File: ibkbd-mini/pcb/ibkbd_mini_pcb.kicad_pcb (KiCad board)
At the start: 2 copper layers, 226 x 106.3 mm, 75 parts

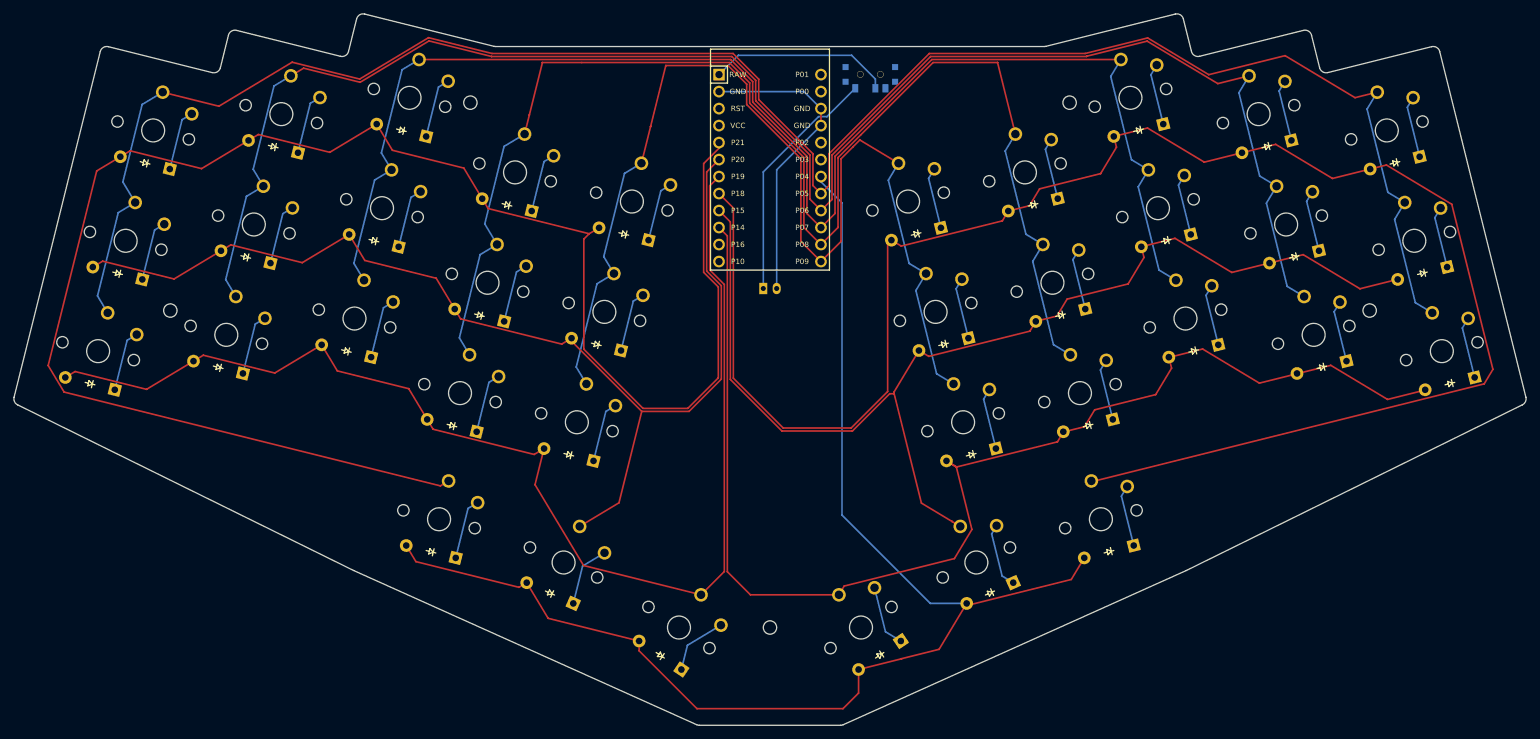
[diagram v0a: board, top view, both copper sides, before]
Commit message: reverse diode direction
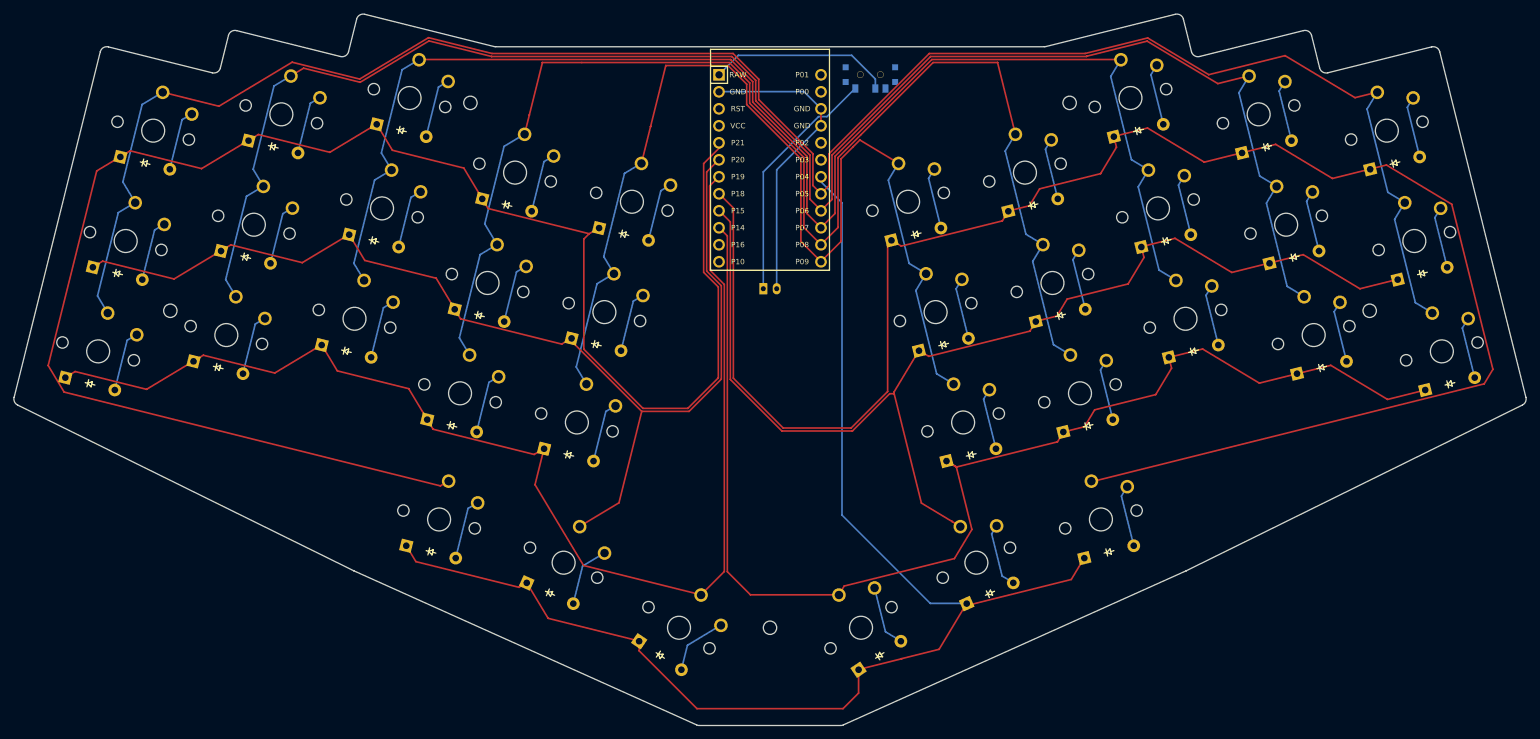
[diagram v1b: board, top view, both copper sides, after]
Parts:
- turned D18 to 14 degrees
- turned D36 to 34 degrees
- turned D33 to -34 degrees
- turned D21 to 14 degrees
- turned D25 to 14 degrees
- turned D11 to -14 degrees
- turned D34 to 14 degrees
- turned D35 to 24 degrees
- turned D15 to -14 degrees
- turned D1 to -14 degrees
- turned D20 to 14 degrees
- turned D19 to 14 degrees
- turned D32 to -24 degrees
- turned D4 to -14 degrees
- turned D24 to 14 degrees
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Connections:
- D1 pad 1: pinky_bottom -> P19
- D1 pad 2: P19 -> pinky_bottom
- D10 pad 1: index_bottom -> P19
- D10 pad 2: P19 -> index_bottom
- D11 pad 1: index_home -> P20
- D11 pad 2: P20 -> index_home
- D12 pad 1: index_top -> P21
- D12 pad 2: P21 -> index_top
- D13 pad 1: inner_bottom -> P19
- D13 pad 2: P19 -> inner_bottom
- D14 pad 1: inner_home -> P20
- D14 pad 2: P20 -> inner_home
- D15 pad 1: inner_top -> P21
- D15 pad 2: P21 -> inner_top
- D16 pad 1: mirror_pinky_bottom -> P14
- D16 pad 2: P14 -> mirror_pinky_bottom
- D17 pad 1: mirror_pinky_home -> P15
- D17 pad 2: P15 -> mirror_pinky_home
- D18 pad 1: mirror_pinky_top -> P18
- D18 pad 2: P18 -> mirror_pinky_top
- D19 pad 1: mirror_ring_bottom -> P14
- D19 pad 2: P14 -> mirror_ring_bottom
- D2 pad 1: pinky_home -> P20
- D2 pad 2: P20 -> pinky_home
- D20 pad 1: mirror_ring_home -> P15
- D20 pad 2: P15 -> mirror_ring_home
- D21 pad 1: mirror_ring_top -> P18
- D21 pad 2: P18 -> mirror_ring_top
- D22 pad 1: mirror_middle_bottom -> P14
- D22 pad 2: P14 -> mirror_middle_bottom
- D23 pad 1: mirror_middle_home -> P15
- D23 pad 2: P15 -> mirror_middle_home
- D24 pad 1: mirror_middle_top -> P18
- D24 pad 2: P18 -> mirror_middle_top
- D25 pad 1: mirror_index_bottom -> P14
- D25 pad 2: P14 -> mirror_index_bottom
- D26 pad 1: mirror_index_home -> P15
- D26 pad 2: P15 -> mirror_index_home
- D27 pad 1: mirror_index_top -> P18
- D27 pad 2: P18 -> mirror_index_top
- D28 pad 1: mirror_inner_bottom -> P14
- D28 pad 2: P14 -> mirror_inner_bottom
- D29 pad 1: mirror_inner_home -> P15
- D29 pad 2: P15 -> mirror_inner_home
- D3 pad 1: pinky_top -> P21
- D3 pad 2: P21 -> pinky_top
- D30 pad 1: mirror_inner_top -> P18
- D30 pad 2: P18 -> mirror_inner_top
- D31 pad 1: inner_key -> P4
- D31 pad 2: P4 -> inner_key
- D32 pad 1: mid_key -> P4
- D32 pad 2: P4 -> mid_key
- D33 pad 1: outer_key -> P4
- D33 pad 2: P4 -> outer_key
- D34 pad 1: mirror_inner_key -> P4
- D34 pad 2: P4 -> mirror_inner_key
- D35 pad 1: mirror_mid_key -> P4
- D35 pad 2: P4 -> mirror_mid_key
- D36 pad 1: mirror_outer_key -> P4
- D36 pad 2: P4 -> mirror_outer_key
- D4 pad 1: ring_bottom -> P19
- D4 pad 2: P19 -> ring_bottom
- D5 pad 1: ring_home -> P20
- D5 pad 2: P20 -> ring_home
- D6 pad 1: ring_top -> P21
- D6 pad 2: P21 -> ring_top
- D7 pad 1: middle_bottom -> P19
- D7 pad 2: P19 -> middle_bottom
- D8 pad 1: middle_home -> P20
- D8 pad 2: P20 -> middle_home
- D9 pad 1: middle_top -> P21
- D9 pad 2: P21 -> middle_top

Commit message: fix diode direction on thumb keys, update routed pcb
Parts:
- moved S23 41.9 mm to (231.2, 99.9)
- moved S27 41.9 mm to (211.4, 94.5)
- moved S14 41.9 mm to (148.5, 115.4)
- moved S17 41.9 mm to (269.6, 104.7)
- moved S20 41.9 mm to (250.4, 102.3)
- moved D3 41.9 mm to (79.9, 93.1)
- moved D32 41.9 mm to (140.4, 157.4), turned to 156 degrees
- moved D35 41.9 mm to (206.1, 157.4), turned to -156 degrees
- moved S33 41.9 mm to (159.7, 162.5)
- moved S36 41.9 mm to (186.9, 162.5)
- moved D14 41.9 mm to (147.3, 120.2)
- moved D17 41.9 mm to (270.8, 109.6)
- moved D19 41.9 mm to (255.7, 123.6)
- moved D21 41.9 mm to (247.5, 90.6)
- moved D22 41.9 mm to (236.6, 121.2)
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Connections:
- D31 pad 1: P4 -> inner_key
- D31 pad 2: inner_key -> P4
- D32 pad 1: P4 -> mid_key
- D32 pad 2: mid_key -> P4
- D33 pad 1: P4 -> outer_key
- D33 pad 2: outer_key -> P4
- D34 pad 1: P4 -> mirror_inner_key
- D34 pad 2: mirror_inner_key -> P4
- D35 pad 1: P4 -> mirror_mid_key
- D35 pad 2: mirror_mid_key -> P4
- D36 pad 1: P4 -> mirror_outer_key
- D36 pad 2: mirror_outer_key -> P4

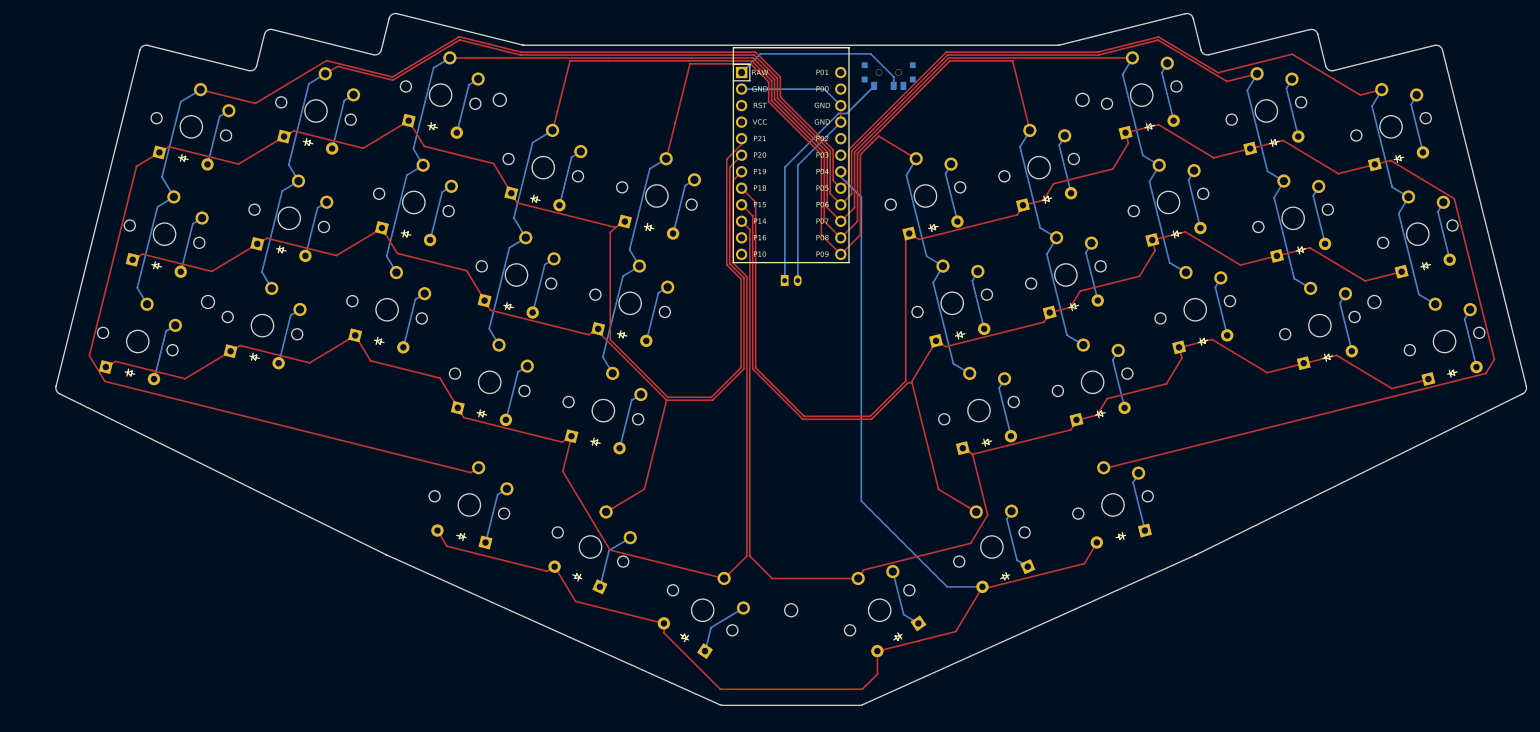
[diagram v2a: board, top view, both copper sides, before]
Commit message: update pcb to use hotswap choc switches
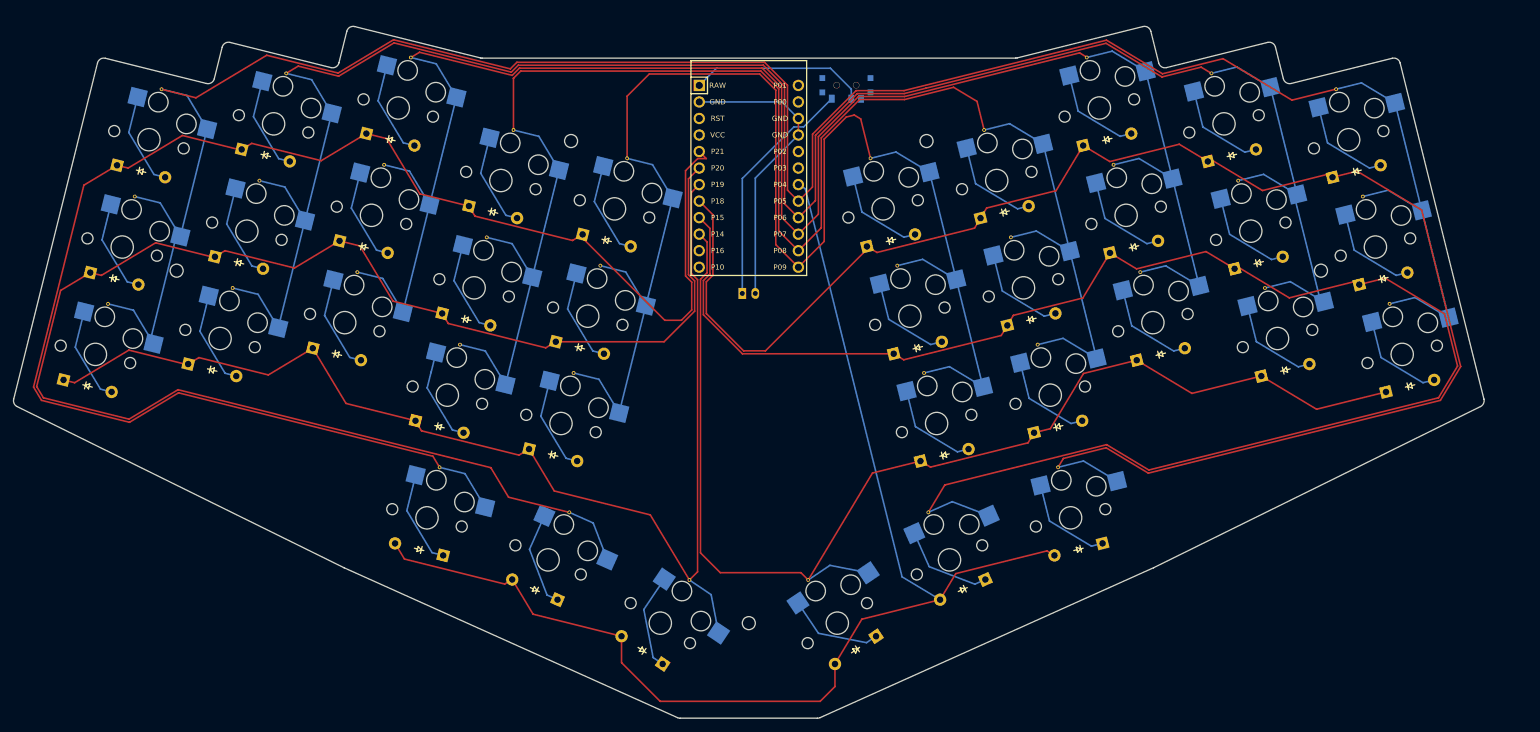
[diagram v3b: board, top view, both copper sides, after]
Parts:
- removed the S13 at (144.4, 131.8)
- added REF**: VIA-0.6mm, VIA-0.6mm, F.Cu at (91.5, 96.5)
- added REF**: VIA-0.6mm, VIA-0.6mm, F.Cu at (207.0, 105.2)
- added REF**: VIA-0.6mm, VIA-0.6mm, F.Cu at (242.0, 96.5)
- added REF**: VIA-0.6mm, VIA-0.6mm, F.Cu at (222.8, 94.1)
- added REF**: VIA-0.6mm, VIA-0.6mm, F.Cu at (143.9, 109.6)
- added REF**: VIA-0.6mm, VIA-0.6mm, F.Cu at (126.5, 105.2)
- added REF**: VIA-0.6mm, VIA-0.6mm, F.Cu at (106.6, 110.6)
- added REF**: VIA-0.6mm, VIA-0.6mm, F.Cu at (139.2, 147.5)
- added REF**: VIA-0.6mm, VIA-0.6mm, F.Cu at (148.0, 93.1)
- added REF**: VIA-0.6mm, VIA-0.6mm, F.Cu at (202.9, 88.7)
- added REF**: VIA-0.6mm, VIA-0.6mm, F.Cu at (194.3, 147.5)
- added REF**: VIA-0.6mm, VIA-0.6mm, F.Cu at (237.8, 80.0)
- added REF**: VIA-0.6mm, VIA-0.6mm, F.Cu at (265.2, 115.4)
- added REF**: VIA-0.6mm, VIA-0.6mm, F.Cu at (226.9, 110.6)
- added REF**: VIA-0.6mm, VIA-0.6mm, F.Cu at (87.4, 113.0)
- added REF**: VIA-0.6mm, VIA-0.6mm, F.Cu at (110.7, 94.1)
- added REF**: VIA-0.6mm, VIA-0.6mm, F.Cu at (185.5, 93.1)
- added REF**: VIA-0.6mm, VIA-0.6mm, F.Cu at (257.0, 82.4)
- added REF**: VIA-0.6mm, VIA-0.6mm, F.Cu at (193.7, 126.1)
- added REF**: VIA-0.6mm, VIA-0.6mm, F.Cu at (211.1, 121.7)
- added REF**: VIA-0.6mm, VIA-0.6mm, F.Cu at (214.3, 140.6)
- added REF**: VIA-0.6mm, VIA-0.6mm, F.Cu at (261.1, 98.9)
- added REF**: VIA-0.6mm, VIA-0.6mm, F.Cu at (95.6, 80.0)
- added REF**: VIA-0.6mm, VIA-0.6mm, F.Cu at (157.6, 157.9)
- added REF**: VIA-0.6mm, VIA-0.6mm, F.Cu at (246.1, 113.0)
- added REF**: VIA-0.6mm, VIA-0.6mm, F.Cu at (114.8, 77.6)
- added REF**: VIA-0.6mm, VIA-0.6mm, F.Cu at (130.6, 88.7)
- added REF**: VIA-0.6mm, VIA-0.6mm, F.Cu at (122.4, 121.7)
- added REF**: VIA-0.6mm, VIA-0.6mm, F.Cu at (175.9, 157.9)
- added REF**: VIA-0.6mm, VIA-0.6mm, F.Cu at (72.4, 98.9)
- added REF**: VIA-0.6mm, VIA-0.6mm, F.Cu at (139.8, 126.1)
- added REF**: VIA-0.6mm, VIA-0.6mm, F.Cu at (189.6, 109.6)
- added REF**: VIA-0.6mm, VIA-0.6mm, F.Cu at (76.5, 82.4)
- added REF**: VIA-0.6mm, VIA-0.6mm, F.Cu at (119.2, 140.6)
- added S1: , PG1350, F.Cu at (66.3, 123.2)
- added S25: , PG1350, F.Cu at (213.1, 129.5)
- added S8: , PG1350, F.Cu at (108.8, 101.8)
- REF**: renamed from S8; value (none) -> VIA-0.6mm; footprint PG1350 -> VIA-0.6mm
- REF**: renamed from S1; value (none) -> VIA-0.6mm; footprint PG1350 -> VIA-0.6mm
- moved REF** 105.8 mm to (218.7, 77.6), turned to 14 degrees
- moved S13 82.0 mm to (137.9, 133.8), turned to -14 degrees
- moved REF** 7.38 mm to (68.3, 115.4)
- moved D4 6.81 mm to (84.3, 125.6)
- moved D27 6.81 mm to (206.1, 101.3)
- moved JST1 6.81 mm to (166.7, 113.8)
- moved D15 6.81 mm to (144.9, 105.7)
- moved S6 6.81 mm to (93.7, 87.8)
- moved D35 6.81 mm to (199.6, 159.4)
- moved D2 6.81 mm to (69.2, 111.6)
- moved D22 6.81 mm to (230.1, 123.2)
- moved D9 6.81 mm to (111.7, 90.2)
- moved D20 6.81 mm to (245.1, 109.1)
- moved D17 6.81 mm to (264.3, 111.6)
- moved D5 6.81 mm to (88.4, 109.1)
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- renumbered S25 to S13
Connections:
- REF** pad 1: middle_home -> P7
- REF** pad 1: pinky_bottom -> P5
- S13 pad 1: mirror_index_bottom -> inner_bottom
- S13 pad 2: P8 -> P9
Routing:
- net P15: track 169.7 -> 252.3 mm
- net P20: track 166.3 -> 247.5 mm
- net P9: track 161.7 -> 226.5 mm
- net P7: track 212.5 -> 272.3 mm
- net P6: track 251.6 -> 310.6 mm
- net P5: track 289.9 -> 348.7 mm
- net P8: track 202.0 -> 255.2 mm
- net P21: track 261.1 -> 247.6 mm
- net P18: track 264.8 -> 252.9 mm
- net index_bottom: track 9.29 -> 14.9 mm
- net middle_top: track 9.29 -> 14.9 mm
- net mirror_ring_home: track 9.29 -> 14.9 mm
- net mirror_pinky_top: track 9.29 -> 14.9 mm
- net mirror_middle_top: track 9.29 -> 14.9 mm
- net mirror_inner_bottom: track 9.29 -> 14.9 mm
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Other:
- outline, holes or cut-outs redrawn

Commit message: udpate tracks and position of slider
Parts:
- moved D23 47.2 mm to (263.4, 135.4)
- moved S23 47.2 mm to (262.2, 130.6)
- moved D18 47.2 mm to (297.6, 123.8)
- moved D11 47.2 mm to (160.7, 146.6)
- moved S34 47.2 mm to (253.6, 177.1)
- moved D24 47.2 mm to (259.3, 118.9)
- moved REF** 47.2 mm to (240.3, 117.5)
- moved REF** 47.2 mm to (302.7, 144.2)
- moved D29 47.2 mm to (230.1, 150.9)
- moved S14 47.2 mm to (179.4, 146.1)
- moved S27 47.2 mm to (242.3, 125.2)
- moved REF** 47.2 mm to (248.6, 150.4)
- moved REF** 47.2 mm to (185.5, 121.8)
- moved REF** 47.2 mm to (156.6, 169.3)
- moved S1 47.2 mm to (103.7, 151.9)
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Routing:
- net P18: track 252.9 -> 249.1 mm
- net P9: track 226.5 -> 223.8 mm
- net P8: track 255.2 -> 252.7 mm
- net P19: track 188.4 -> 190.7 mm
- net batswitch: track 36.5 -> 38.5 mm
- net RAW: track 27.3 -> 28.4 mm
- net P14: track 186.7 -> 187.8 mm
- net P7: track 272.3 -> 271.6 mm
- net P6: track 310.6 -> 309.9 mm
- net P5: track 348.7 -> 348.0 mm
